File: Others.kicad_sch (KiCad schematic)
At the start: 15 parts, among them J16 UFL, J17 IO1, J18 IO2, Q13 SI2312BDS

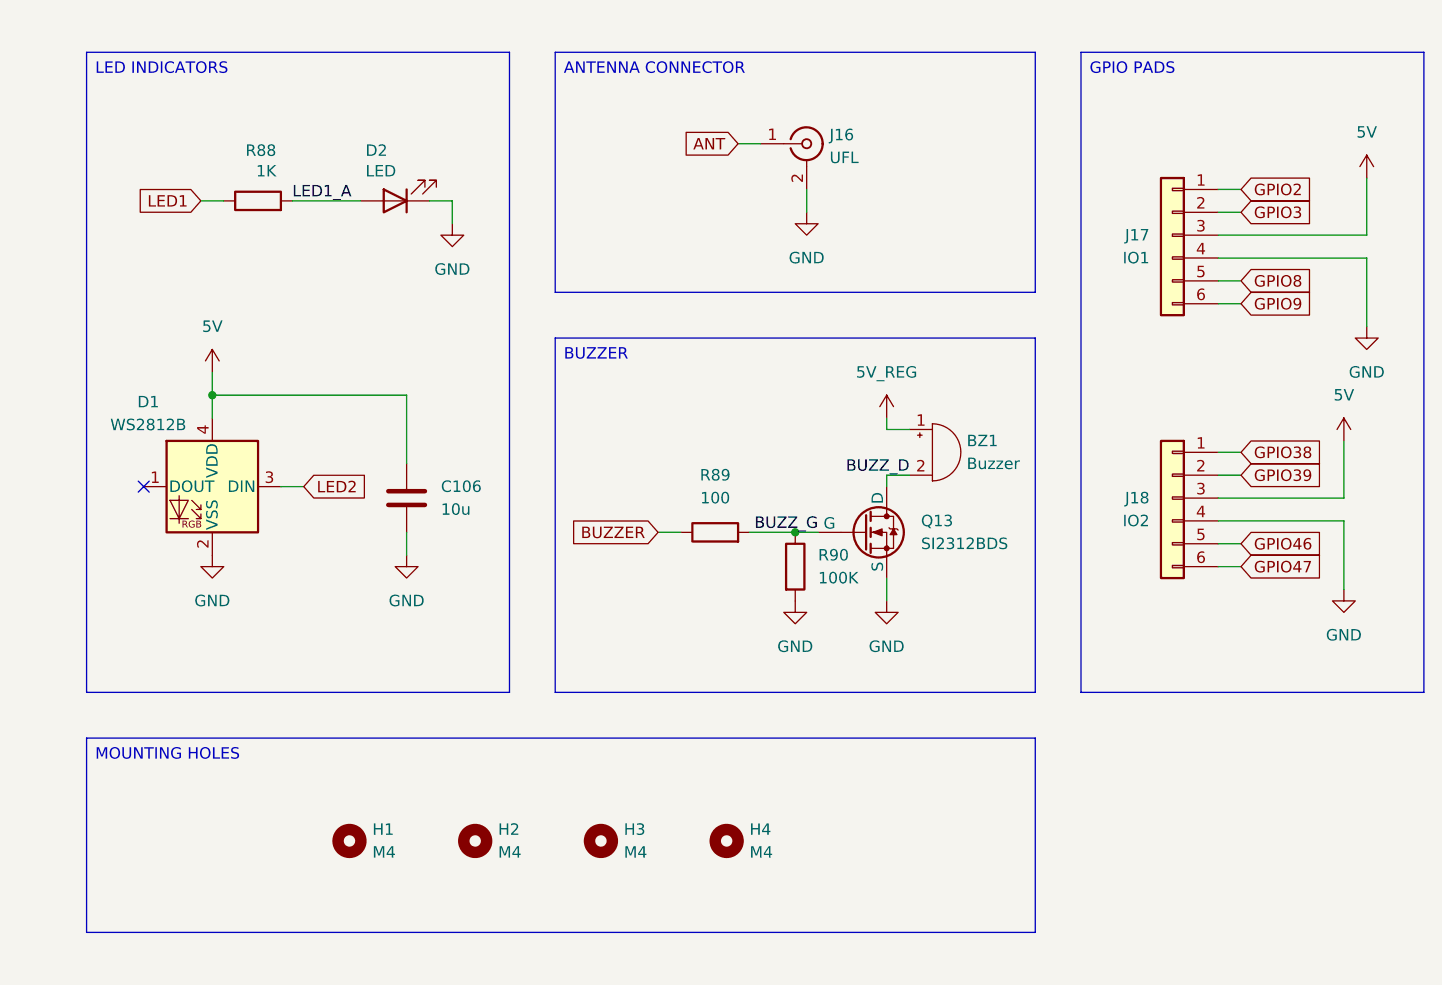
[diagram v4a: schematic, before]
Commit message: MCU layout
Updated the schematic labels.
Continued the MCU layout.
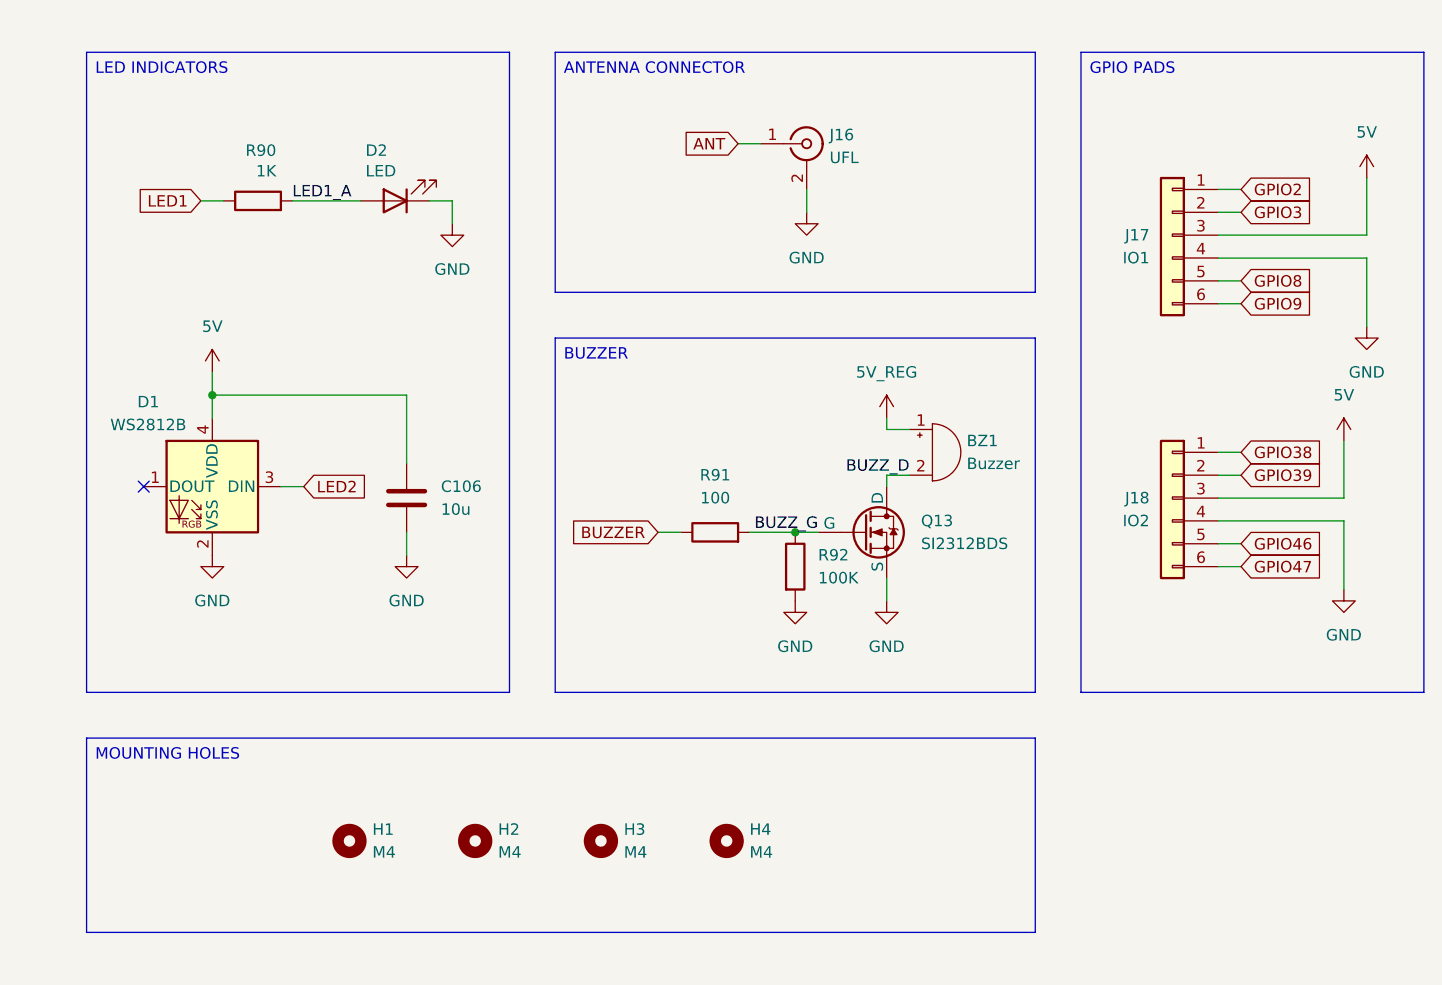
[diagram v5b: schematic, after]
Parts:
- renumbered R88 to R90, R89 to R91, R90 to R92
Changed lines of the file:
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@@
 		(on_board yes)
 		(dnp no)
-		(property "Reference" "#PWR0203"
+		(property "Reference" "#PWR0205"
 			(at 119.38 68.58 0)
 			(effects
@@
 			(project "ThunderHorse"
 				(path "/ac187c6c-fa53-41cc-bce1-6f39a42a92e8/111cf19a-e0f8-4ba5-b5cb-1102d2b05aed"
-					(reference "#PWR0203")
+					(reference "#PWR0205")
 					(unit 1)
 				)
@@
 		(dnp no)
 		(fields_autoplaced yes)
-		(property "Reference" "#PWR0204"
+		(property "Reference" "#PWR0206"
 			(at 157.48 110.49 0)
 			(effects
@@
 			(project "ThunderHorse"
 				(path "/ac187c6c-fa53-41cc-bce1-6f39a42a92e8/111cf19a-e0f8-4ba5-b5cb-1102d2b05aed"
-					(reference "#PWR0204")
+					(reference "#PWR0206")
 					(unit 1)
 				)
@@
 		(dnp no)
 		(fields_autoplaced yes)
-		(property "Reference" "#PWR0201"
+		(property "Reference" "#PWR0203"
 			(at 92.71 105.41 0)
 			(effects
@@
 			(project "ThunderHorse"
 				(path "/ac187c6c-fa53-41cc-bce1-6f39a42a92e8/111cf19a-e0f8-4ba5-b5cb-1102d2b05aed"
-					(reference "#PWR0201")
+					(reference "#PWR0203")
 					(unit 1)
 				)
@@
 		(dnp no)
 		(fields_autoplaced yes)
-		(property "Reference" "#PWR0202"
+		(property "Reference" "#PWR0204"
 			(at 114.3 105.41 0)
 			(effects
@@
 			(project "ThunderHorse"
 				(path "/ac187c6c-fa53-41cc-bce1-6f39a42a92e8/111cf19a-e0f8-4ba5-b5cb-1102d2b05aed"
-					(reference "#PWR0202")
+					(reference "#PWR0204")
 					(unit 1)
 				)
@@
 		(dnp no)
 		(fields_autoplaced yes)
-		(property "Reference" "#PWR0205"
+		(property "Reference" "#PWR0207"
 			(at 158.75 67.31 0)
 			(effects
@@
 			(project "ThunderHorse"
 				(path "/ac187c6c-fa53-41cc-bce1-6f39a42a92e8/111cf19a-e0f8-4ba5-b5cb-1102d2b05aed"
-					(reference "#PWR0205")
+					(reference "#PWR0207")
 					(unit 1)
 				)
@@
 		(on_board yes)
 		(dnp no)
-		(property "Reference" "#PWR0206"
+		(property "Reference" "#PWR0208"
 			(at 167.64 87.63 0)
 			(effects
@@
 			(project "ThunderHorse"
 				(path "/ac187c6c-fa53-41cc-bce1-6f39a42a92e8/111cf19a-e0f8-4ba5-b5cb-1102d2b05aed"
-					(reference "#PWR0206")
+					(reference "#PWR0208")
 					(unit 1)
 				)
@@
 		(dnp no)
 		(fields_autoplaced yes)
-		(property "Reference" "R89"
+		(property "Reference" "R91"
 			(at 148.59 90.17 90)
 			(effects
@@
 			(project "ThunderHorse"
 				(path "/ac187c6c-fa53-41cc-bce1-6f39a42a92e8/111cf19a-e0f8-4ba5-b5cb-1102d2b05aed"
-					(reference "R89")
+					(reference "R91")
 					(unit 1)
 				)
@@
 		(on_board yes)
 		(dnp no)
-		(property "Reference" "#PWR0210"
+		(property "Reference" "#PWR0212"
 			(at 220.98 60.96 0)
 			(effects
@@
 			(project "ThunderHorse"
 				(path "/ac187c6c-fa53-41cc-bce1-6f39a42a92e8/111cf19a-e0f8-4ba5-b5cb-1102d2b05aed"
-					(reference "#PWR0210")
+					(reference "#PWR0212")
 					(unit 1)
 				)
@@
 		(on_board yes)
 		(dnp no)
-		(property "Reference" "#PWR0208"
+		(property "Reference" "#PWR0210"
 			(at 218.44 90.17 0)
 			(effects
@@
 			(project "ThunderHorse"
 				(path "/ac187c6c-fa53-41cc-bce1-6f39a42a92e8/111cf19a-e0f8-4ba5-b5cb-1102d2b05aed"
-					(reference "#PWR0208")
+					(reference "#PWR0210")
 					(unit 1)
 				)
@@
 		(on_board yes)
 		(dnp no)
-		(property "Reference" "R88"
+		(property "Reference" "R90"
 			(at 99.822 54.102 90)
 			(effects
@@
 			(project "ThunderHorse"
 				(path "/ac187c6c-fa53-41cc-bce1-6f39a42a92e8/111cf19a-e0f8-4ba5-b5cb-1102d2b05aed"
-					(reference "R88")
+					(reference "R90")
 					(unit 1)
 				)
@@
 		(dnp no)
 		(fields_autoplaced yes)
-		(property "Reference" "R90"
+		(property "Reference" "R92"
 			(at 160.02 99.0599 0)
 			(effects
@@
 			(project "ThunderHorse"
 				(path "/ac187c6c-fa53-41cc-bce1-6f39a42a92e8/111cf19a-e0f8-4ba5-b5cb-1102d2b05aed"
-					(reference "R90")
+					(reference "R92")
 					(unit 1)
 				)
@@
 		(dnp no)
 		(fields_autoplaced yes)
-		(property "Reference" "#PWR0207"
+		(property "Reference" "#PWR0209"
 			(at 167.64 110.49 0)
 			(effects
@@
 			(project "ThunderHorse"
 				(path "/ac187c6c-fa53-41cc-bce1-6f39a42a92e8/111cf19a-e0f8-4ba5-b5cb-1102d2b05aed"
-					(reference "#PWR0207")
+					(reference "#PWR0209")
 					(unit 1)
 				)
@@
 		(dnp no)
 		(fields_autoplaced yes)
-		(property "Reference" "#PWR0209"
+		(property "Reference" "#PWR0211"
 			(at 218.44 109.22 0)
 			(effects
@@
 			(project "ThunderHorse"
 				(path "/ac187c6c-fa53-41cc-bce1-6f39a42a92e8/111cf19a-e0f8-4ba5-b5cb-1102d2b05aed"
-					(reference "#PWR0209")
+					(reference "#PWR0211")
 					(unit 1)
 				)
@@
 		(dnp no)
 		(fields_autoplaced yes)
-		(property "Reference" "#PWR0211"
+		(property "Reference" "#PWR0213"
 			(at 220.98 80.01 0)
 			(effects
@@
 			(project "ThunderHorse"
 				(path "/ac187c6c-fa53-41cc-bce1-6f39a42a92e8/111cf19a-e0f8-4ba5-b5cb-1102d2b05aed"
-					(reference "#PWR0211")
+					(reference "#PWR0213")
 					(unit 1)
 				)
@@
 		(on_board yes)
 		(dnp no)
-		(property "Reference" "#PWR0200"
+		(property "Reference" "#PWR0202"
 			(at 92.71 82.55 0)
 			(effects
@@
 			(project "ThunderHorse"
 				(path "/ac187c6c-fa53-41cc-bce1-6f39a42a92e8/111cf19a-e0f8-4ba5-b5cb-1102d2b05aed"
-					(reference "#PWR0200")
-					(unit 1)
-				)
+					(reference "#PWR0202")
+					(unit 1)
+				)

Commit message: Schematic revision
Added an ESP32 C3 for the ELRS receiver.
Updated the protection approach for the board.
Updated the net nodes.
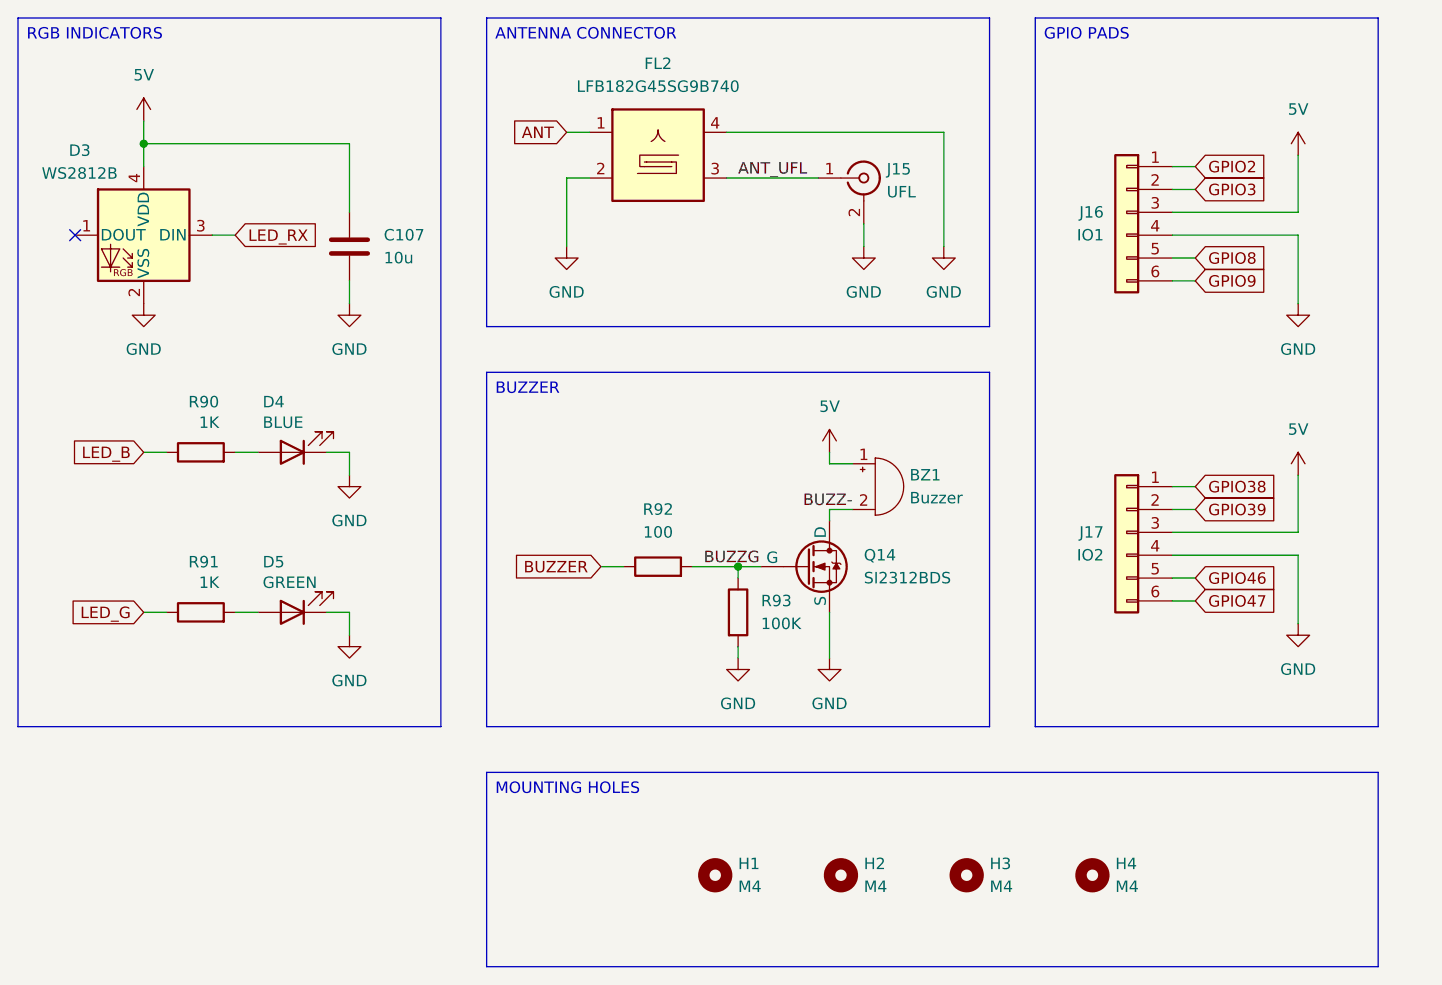
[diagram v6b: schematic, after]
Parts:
- removed C106: 10u, Capacitor_SMD:C_0805_2012Metric, symbol Device:C
- removed D1: WS2812B, Custom_Parts:WS2812B-2020, symbol LED:WS2812B-2020
- added C107: 10u, Capacitor_SMD:C_0805_2012Metric, symbol Device:C
- added D3: WS2812B, Custom_Parts:WS2812B-2020, symbol LED:WS2812B-2020
- added D5: GREEN, LED_SMD:LED_0805_2012Metric, symbol Device:LED
- added FL2: LFB182G45SG9B740, Custom_Parts:LFB182G45SG9B740, symbol Custom_Parts:LFB182G45SG9B740
- added R91: 1K, Resistor_SMD:R_0603_1608Metric, symbol Device:R
- D4: renamed from D2; value LED -> BLUE
- renumbered J16 to J15, J17 to J16, J18 to J17, Q13 to Q14, R91 to R92, R92 to R93
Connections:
- net 5V_REG is gone; now on net 5V: BZ1.1 (+)
- net 5V: now also C107.1, D3.4 (VDD)
- net ANT: now also FL2.1; no longer J15.1 (In)
- net GND: now also C107.2, D3.2 (VSS), D5.1 (K), FL2.2, FL2.4
- net BUZZ_D renamed BUZZ-
- net BUZZ_G renamed BUZZG
- net LED1 renamed LED_B
- net LED1_A: no longer names the net of D4.2 (A), R90.2
- new net: D5.2 (A), R91.2
- new net ANT_UFL: FL2.3, J15.1 (In)
- new net LED_G: R91.1
- new net LED_RX: D3.3 (DIN)
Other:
- moved on the sheet: BZ1, D4, H1, H2, H3, H4, J15, J16, J17, Q14, R90, R92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

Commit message: Schematic and PCB
Reviewed the schematic and deleted unused components.
Updated the PCB and also removed unused footprints.
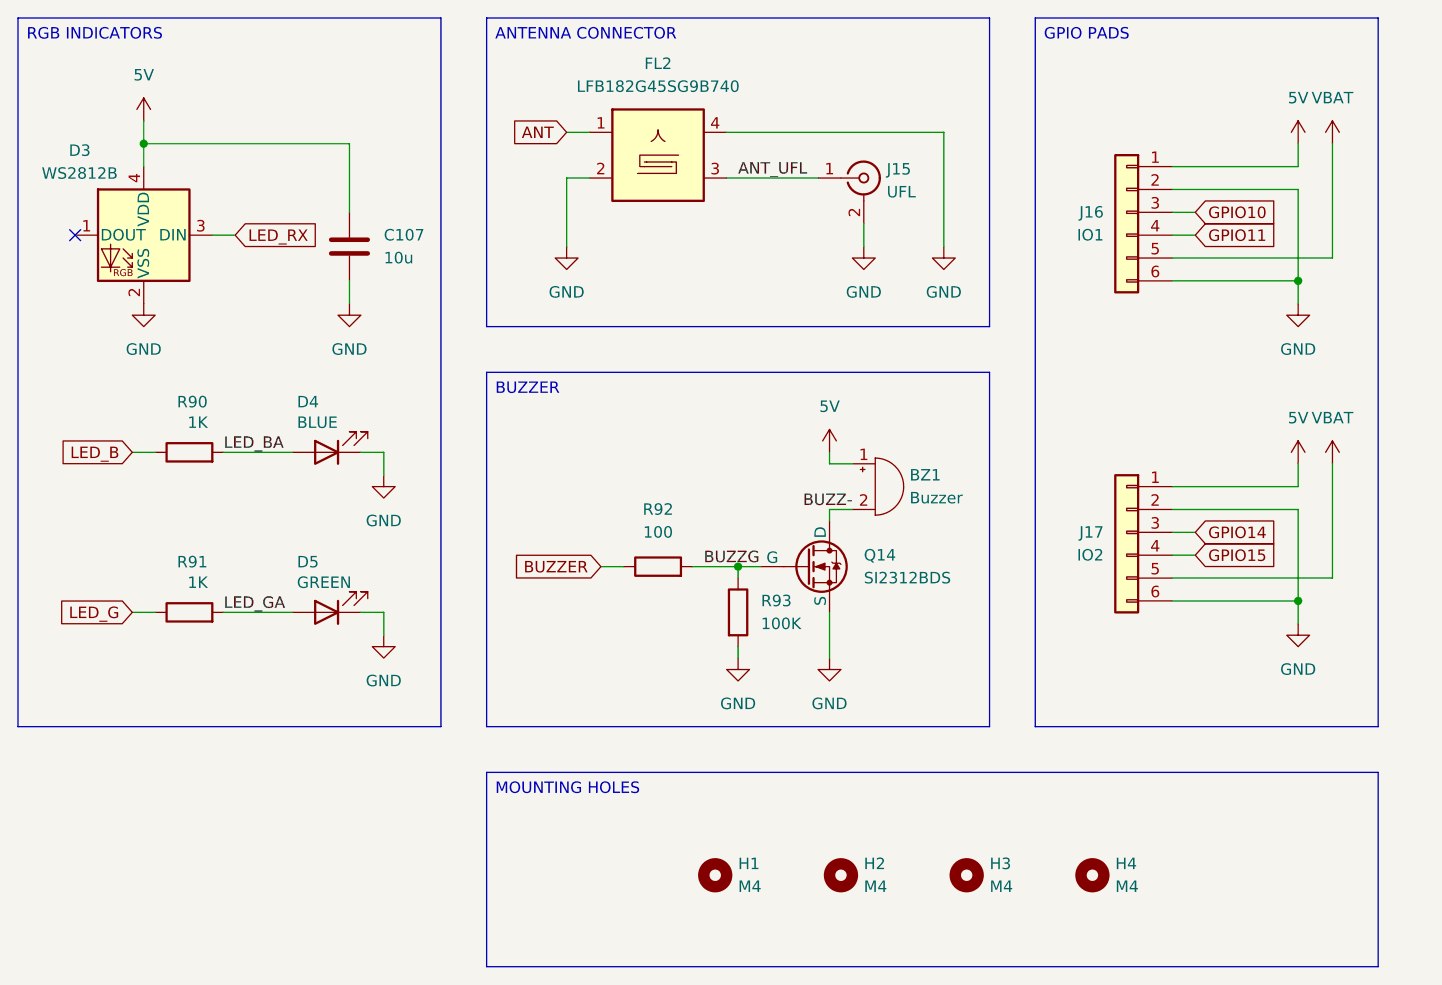
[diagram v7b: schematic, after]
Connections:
- net GPIO2 is gone; now on net 5V: J16.1 (Pin_1)
- net GPIO3 is gone; now on net GND: J16.2 (Pin_2)
- net GPIO38 is gone; now on net 5V: J17.1 (Pin_1)
- net GPIO39 is gone; now on net GND: J17.2 (Pin_2)
- net GPIO47 is gone; now on net GND: J17.6 (Pin_6)
- net GPIO8 is gone; now on net VBAT: J16.5 (Pin_5)
- net GPIO9 is gone; now on net GND: J16.6 (Pin_6)
- net 5V: no longer J16.3 (Pin_3), J17.3 (Pin_3)
- net GND: no longer J16.4 (Pin_4), J17.4 (Pin_4)
- net LED_BA: now reaches D4.2 (A), R90.2
- net LED_GA: now reaches D5.2 (A), R91.2
- net GPIO46 renamed VBAT
- new net GPIO10: J16.3 (Pin_3)
- new net GPIO11: J16.4 (Pin_4)
- new net GPIO14: J17.3 (Pin_3)
- new net GPIO15: J17.4 (Pin_4)
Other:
- moved on the sheet: D4, D5, R90, R91
